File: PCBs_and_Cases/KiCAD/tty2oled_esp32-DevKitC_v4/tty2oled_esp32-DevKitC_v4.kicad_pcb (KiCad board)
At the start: 2 copper layers, 35.6 x 99.7 mm, 2 parts

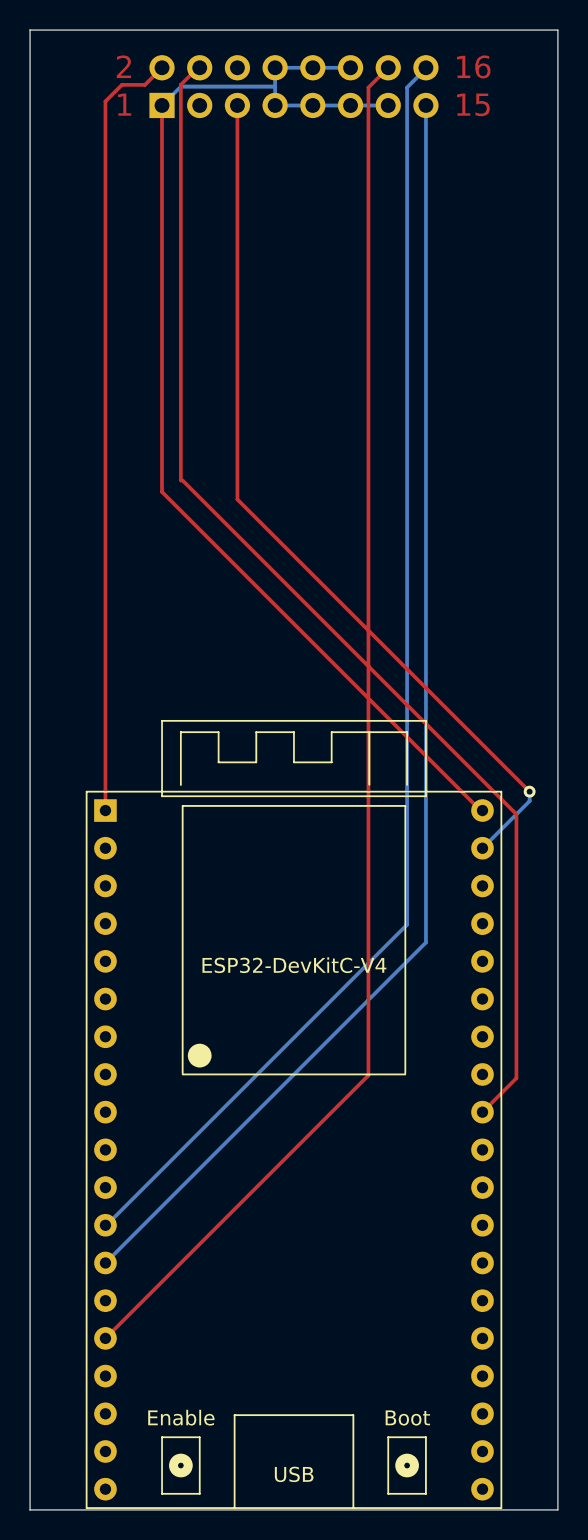
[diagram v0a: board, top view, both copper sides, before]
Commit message: Fixed shortcut in esp32-DevKitC_v4 design
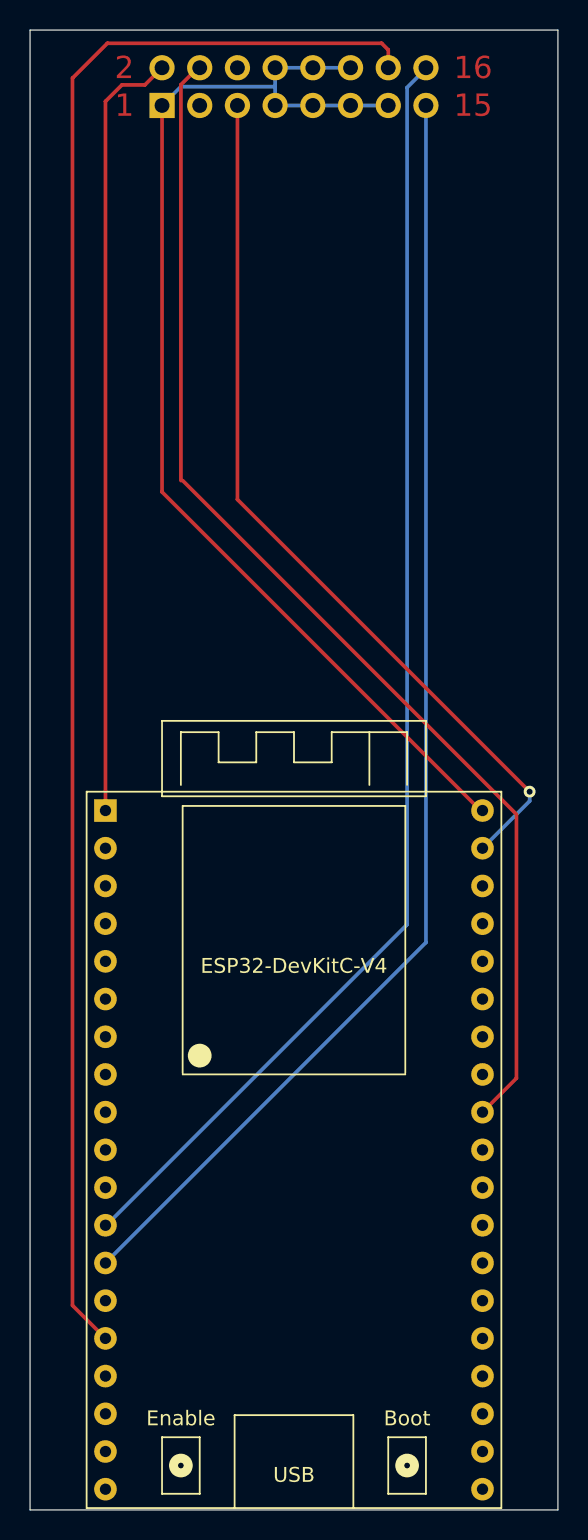
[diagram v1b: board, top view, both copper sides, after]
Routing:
- net (no net): track 540.6 -> 556.6 mm
